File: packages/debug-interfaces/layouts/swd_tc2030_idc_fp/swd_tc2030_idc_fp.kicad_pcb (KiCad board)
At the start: 2 copper layers, 1 part

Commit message: Update build script and regenerate outputs
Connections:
- U1 pad 2: line-1 -> line-3
- U1 pad 3: line-3 -> line
- U1 pad 4: line-2 -> line-1
- U1 pad 6: line -> line-2
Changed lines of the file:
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@@
     )
     (net 0 "")
-    (net 1 "line-3")
+    (net 1 "line")
     (net 2 "gnd")
-    (net 3 "line-1")
-    (net 4 "line")
-    (net 5 "line-2")
+    (net 3 "line-3")
+    (net 4 "line-2")
+    (net 5 "line-1")
     (net 6 "hv")
     (footprint "Connector:Tag-Connect_TC2030-IDC-FP_2x03_P1.27mm_Vertical"
@@
             (size 0.7874 0.7874)
             (layers "F.Cu" "F.Mask")
-            (net 3 "line-1")
+            (net 3 "line-3")
         )
         (pad "3" connect circle
@@
             (size 0.7874 0.7874)
             (layers "F.Cu" "F.Mask")
-            (net 1 "line-3")
+            (net 1 "line")
         )
         (pad "4" connect circle
@@
             (size 0.7874 0.7874)
             (layers "F.Cu" "F.Mask")
-            (net 5 "line-2")
+            (net 5 "line-1")
         )
         (pad "5" connect circle
@@
             (size 0.7874 0.7874)
             (layers "F.Cu" "F.Mask")
-            (net 4 "line")
+            (net 4 "line-2")
         )
         (embedded_fonts no)

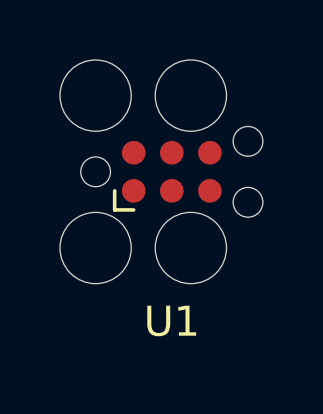
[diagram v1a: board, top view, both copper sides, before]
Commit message: Build all packages without designators on silkscreen.
Also disable fail_on_drc and enable keep_picked_parts for build
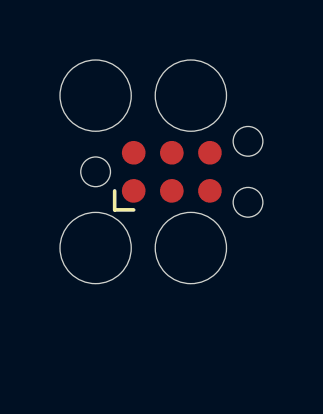
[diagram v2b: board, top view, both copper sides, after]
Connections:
- U1 pad 2: line-3 -> line-2
- U1 pad 4: line-1 -> line-3
- U1 pad 6: line-2 -> line-1
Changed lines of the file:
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@@
     (net 1 "line")
     (net 2 "gnd")
-    (net 3 "line-3")
-    (net 4 "line-2")
-    (net 5 "line-1")
+    (net 3 "line-2")
+    (net 4 "line-1")
+    (net 5 "line-3")
     (net 6 "hv")
     (footprint "Connector:Tag-Connect_TC2030-IDC-FP_2x03_P1.27mm_Vertical"
@@
             (at 0 5 0)
             (layer "F.SilkS")
-            (hide no)
+            (hide yes)
             (effects
                 (font
@@
                     (thickness 0.15)
                 )
+                (hide yes)
             )
             (unlocked no)
@@
             (size 0.7874 0.7874)
             (layers "F.Cu" "F.Mask")
-            (net 3 "line-3")
+            (net 3 "line-2")
         )
         (pad "3" connect circle
@@
             (size 0.7874 0.7874)
             (layers "F.Cu" "F.Mask")
-            (net 5 "line-1")
+            (net 5 "line-3")
         )
         (pad "5" connect circle
@@
             (size 0.7874 0.7874)
             (layers "F.Cu" "F.Mask")
-            (net 4 "line-2")
+            (net 4 "line-1")
         )
         (embedded_fonts no)

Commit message: [Publish] Fix image links and rebuild
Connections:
- U1 pad 2: line-2 -> line-1
- U1 pad 3: line -> line-3
- U1 pad 4: line-3 -> line-2
- U1 pad 6: line-1 -> line
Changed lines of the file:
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@@
     )
     (net 0 "")
-    (net 1 "line")
+    (net 1 "line-3")
     (net 2 "gnd")
-    (net 3 "line-2")
-    (net 4 "line-1")
-    (net 5 "line-3")
+    (net 3 "line-1")
+    (net 4 "line")
+    (net 5 "line-2")
     (net 6 "hv")
     (footprint "Connector:Tag-Connect_TC2030-IDC-FP_2x03_P1.27mm_Vertical"
@@
             (size 0.7874 0.7874)
             (layers "F.Cu" "F.Mask")
-            (net 3 "line-2")
+            (net 3 "line-1")
         )
         (pad "3" connect circle
@@
             (size 0.7874 0.7874)
             (layers "F.Cu" "F.Mask")
-            (net 1 "line")
+            (net 1 "line-3")
         )
         (pad "4" connect circle
@@
             (size 0.7874 0.7874)
             (layers "F.Cu" "F.Mask")
-            (net 5 "line-3")
+            (net 5 "line-2")
         )
         (pad "5" connect circle
@@
             (size 0.7874 0.7874)
             (layers "F.Cu" "F.Mask")
-            (net 4 "line-1")
+            (net 4 "line")
         )
         (embedded_fonts no)
